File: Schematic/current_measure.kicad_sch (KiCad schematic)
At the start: 59 parts, among them J1 Conn_01x04_Pin, J2 Screw_Terminal_01x02, J3 Conn_01x02, J4 PowerSupply select, J5 Conn_02x03_Counter_Clockwise, J6 Conn_01x04, Q1 Si2319CDS, SW1 SW_Push, U1 6N137, U2 6N137, U3 INA186, U4 MCP6002-xSN, U5 MIC5365-3.3YD5, U6 STM32G431C8Tx, U7 OPA350, Y1 8MHz

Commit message: Initial PCB
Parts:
- removed R1, R3: 680, Resistor_SMD:R_0805_2012Metric, symbol Device:R
- removed U1, U2: 6N137, Package_DIP:DIP-8_W7.62mm, symbol Isolator:6N137
- added U3: ISO652, Package_SO:SOIC-8_3.9x4.9mm_P1.27mm, symbol Isolator:ISO7721D
- D1, D2: footprint Diode_SMD:D_SMA_Handsoldering -> Diode_SMD:D_SOD-123F
- RV1, RV2: footprint Resistor_SMD:R_0805_2012Metric -> Potentiometer_THT:Potentiometer_Vishay_T73YP_Vertical
- Y1: footprint Filter:Filter_Mini-Circuits_FV1206-7 -> Crystal:Resonator_SMD-3Pin_7.2x3.0mm
- renumbered C17 to C10, C18 to C11, C6 to C12, C7 to C13, C8 to C14, C9 to C15, C10 to C16, C11 to C17, C19 to C18, C15 to C19, C12 to C4, C13 to C5, C14 to C6, C4 to C7, C5 to C8, C16 to C9, J3 to J2, J2 to J3, R2 to R1, R12 to R10, R13 to R11, R14 to R12, R4 to R2, R5 to R3, R6 to R4, R7 to R5, R8 to R6, R9 to R7, R10 to R8, R11 to R9, U5 to U1, U3 to U2, U7 to U5
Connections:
- net +3.3V: now also U3.1 (VCC1)
- net GND: now also U3.4 (GND1)
- net MCU_RxD: now also U3.2 (OUTA)
- net MCU_TxD: now also U3.3 (INB)
- net USB_+5: now also U3.8 (VCC2)
- net USB_GND: now also U3.5 (GND2)
- net USB_RxD: now also U3.6 (OUTB)
- net USB_TxD: now also U3.7 (INA)
- net I_{sense}+: now reaches J3.1 (Pin_1), R1.1, R2.1
- net I_{sense}-: now reaches J3.2 (Pin_2), R2.2, R3.1
- no-connect marks 11 -> 7
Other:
- moved on the sheet: J1

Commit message: PCB small
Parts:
- removed C11: 10µ, Capacitor_SMD:C_0805_2012Metric, symbol Device:C
- removed C22: 1µ, Capacitor_SMD:C_0805_2012Metric, symbol Device:C
- removed C23: 0.1µ, Capacitor_SMD:C_0805_2012Metric, symbol Device:C
- removed C3: 10u, Capacitor_SMD:C_0805_2012Metric, symbol Device:C
- removed J4: PowerSupply select, Connector_PinSocket_2.54mm:PinSocket_1x03_P2.54mm_Vertical, symbol Connector:Conn_01x03_Pin
- removed U4: MCP6002-xSN, Package_SO:SOIC-8_3.9x4.9mm_P1.27mm, symbol Amplifier_Operational:MCP6002-xSN
- added C20: 100n, Capacitor_SMD:C_0805_2012Metric, symbol Device:C
- added JP1: SolderJumper_3_Open, Jumper:SolderJumper-3_P1.3mm_Open_Pad1.0x1.5mm, symbol Jumper:SolderJumper_3_Open
- added U4: OPA333xxDBV, Package_TO_SOT_SMD:SOT-23-5, symbol Amplifier_Operational:OPA333xxDBV
- added U7: OPA333xxDBV, Package_TO_SOT_SMD:SOT-23-5_HandSoldering, symbol Amplifier_Operational:OPA333xxDBV
- RV1, RV2: footprint Potentiometer_THT:Potentiometer_Vishay_T73YP_Vertical -> Potentiometer_THT:Potentiometer_Bourns_3296Z_Horizontal
- Y1: footprint Crystal:Resonator_SMD-3Pin_7.2x3.0mm -> Crystal:Resonator_SMD_Murata_CSTxExxV-3Pin_3.0x1.1mm
- renumbered C12 to C10, C13 to C11, C14 to C12, C15 to C13, C16 to C14, C17 to C15, C18 to C16, C19 to C17, C20 to C18, C21 to C19, C4 to C3, C5 to C4, C6 to C5, C7 to C6, C8 to C7, C9 to C8, C10 to C9
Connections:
- net +3.3V: now also J6.3 (Pin_3), C20.1, U4.2 (V-), U7.2 (V-); no longer J6.4 (Pin_4)
- net +3.3VP: now also JP1.1 (A)
- net +5V: now also JP1.3 (B)
- net GND: now also J6.4 (Pin_4), RV1.1, C20.2, U4.5 (V+), U7.5 (V+); no longer J6.1 (Pin_1), RV1.2, RV1.3
- net MCU_I2C_SDA: now also J6.1 (Pin_1); no longer J6.3 (Pin_3)
- net REF_{offset}: now also U4.1, U4.4 (-)
- net V_{buf}: now also U7.1, U7.4 (-)
- net V_{ref}: now also U7.3 (+)
- net at R4.2: now also RV1.2, RV1.3, U4.3 (+); no longer RV1.1
- net at R5.1, R6.2: now also U5.2 (-); no longer U5.3 (+)
- net V_{prog}: now reaches J5.6 (Pin_6)
- net V_{prog}: now also JP1.2 (C)
- net at R8.2, R9.1, RV2.1: now also U5.3 (+); no longer U5.2 (-)
- net xTAL_{1} renamed xTAL+
- net xTAL_{2} renamed xTAL-
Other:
- note removed: "Zasilanie bufora napięcia referencyjnego"
- moved on the sheet: C8, C9, D3, D4, J6, R11, R12

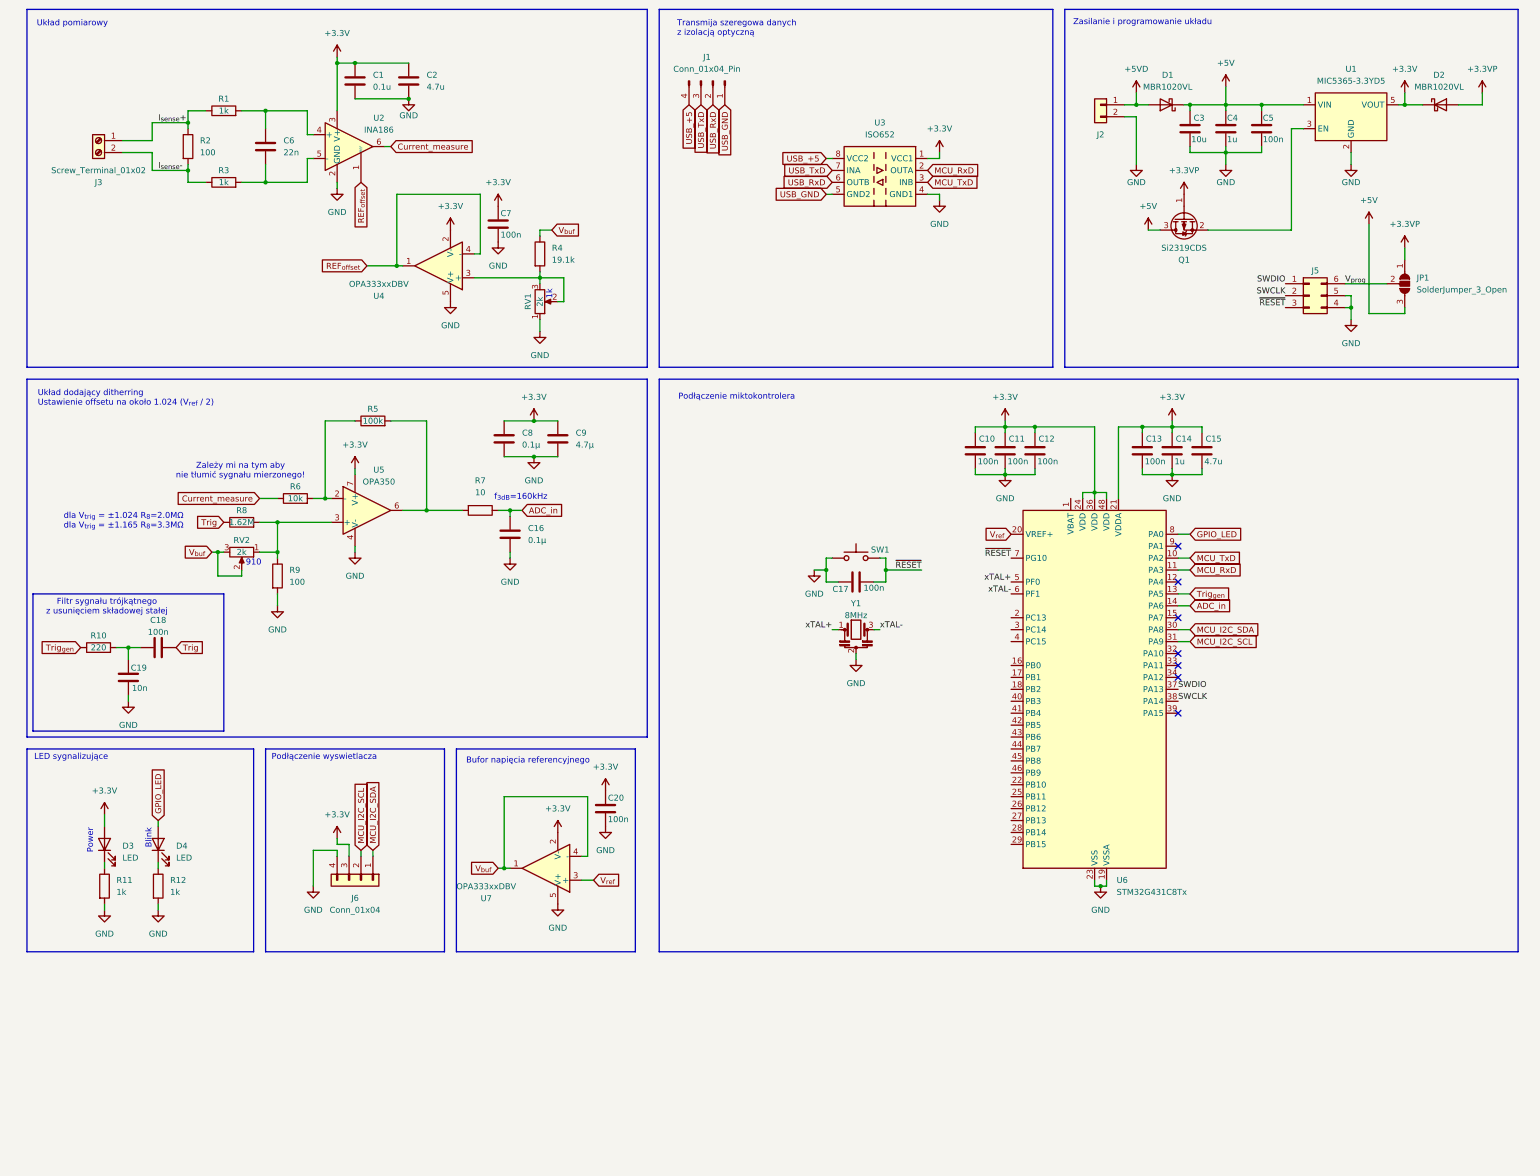
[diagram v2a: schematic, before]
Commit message: Fix small issues with I2C and add power cap
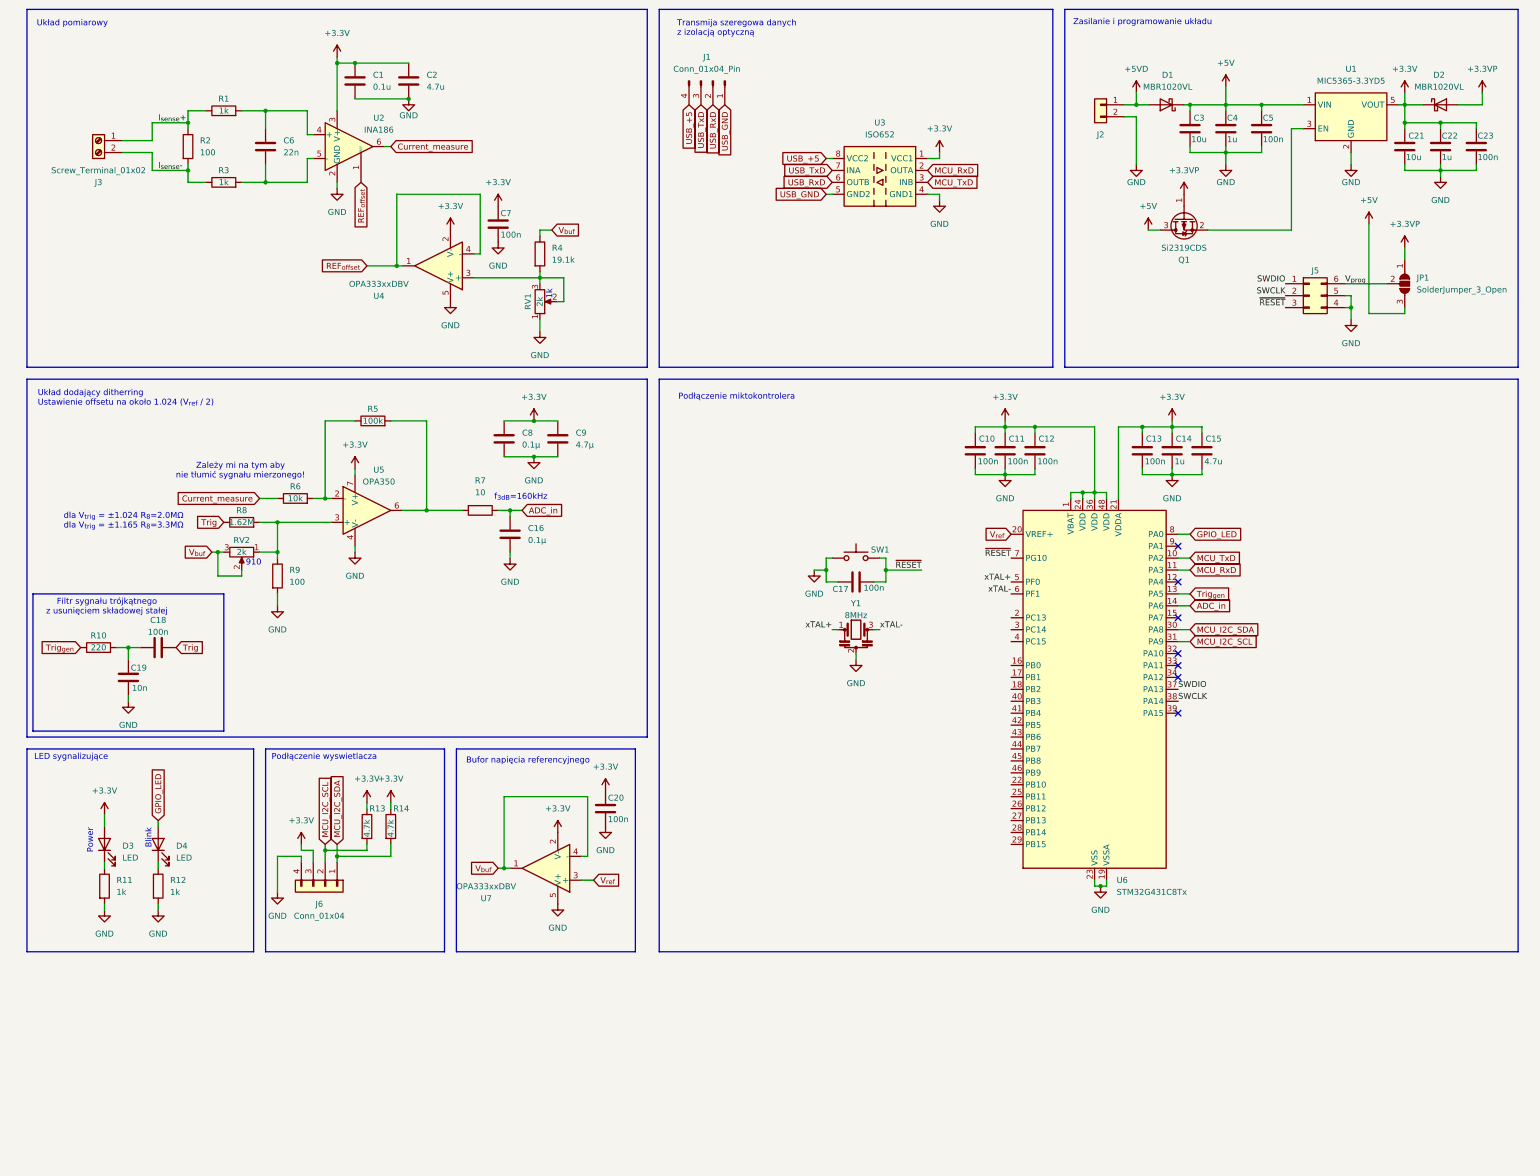
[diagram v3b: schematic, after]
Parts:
- added C21: 10u, Capacitor_SMD:C_0805_2012Metric, symbol Device:C
- added C22: 1u, Capacitor_SMD:C_0805_2012Metric, symbol Device:C
- added C23: 100n, Capacitor_SMD:C_0805_2012Metric, symbol Device:C
- added R13, R14: 4.7k, Resistor_SMD:R_0805_2012Metric, symbol Device:R
- J6: footprint Connector_PinHeader_2.54mm:PinHeader_1x04_P2.54mm_Vertical -> Connector_PinSocket_2.54mm:PinSocket_1x04_P2.54mm_Vertical
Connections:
- net +3.3V: now also U6.1 (VBAT), C21.1, C22.1, C23.1, R13.1, R14.1
- net GND: now also C21.2, C22.2, C23.2
- net MCU_I2C_SCL: now also R13.2
- net MCU_I2C_SDA: now also R14.2
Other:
- moved on the sheet: J6
